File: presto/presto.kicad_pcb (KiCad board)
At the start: 2 copper layers, 110 x 110 mm, 61 parts, among them J101 12V IN, J301 ESTOP IN, J401 ESTOP SW, J701 LED Connector, K301 12V SRD Form C, K401 12V SRD Form C

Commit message: LED diode traces not connected properly, deleted, needs to be fixed
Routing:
- net /LED Interface/green: track 83.4 -> 162.4 mm
- net /LED Interface/yellow: track 83.7 -> 24.5 mm
- net /LED Interface/red: track 77.4 -> 32.7 mm
- net /LED Interface/blue: track 78.3 -> 117.2 mm
- net /EStop Reading/estop_signal: track 79.6 -> 78.7 mm
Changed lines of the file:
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@@
 	)
 	(gr_text "6 mm apart"
-		(at 61.595 139.7 0)
+		(at 55.245 141.605 0)
 		(layer "F.Cu")
 		(effects
@@
 	)
 	(segment
-		(start 123.825 120.65)
-		(end 130.175 120.65)
-		(width 0.2)
-		(layer "B.Cu")
-		(net 1)
-	)
-	(segment
-		(start 130.175 120.65)
-		(end 144.78 135.255)
-		(width 0.2)
-		(layer "B.Cu")
-		(net 1)
-	)
-	(segment
-		(start 108.75 114.3)
-		(end 117.475 114.3)
-		(width 0.2)
-		(layer "B.Cu")
-		(net 1)
-	)
-	(segment
-		(start 117.475 114.3)
-		(end 123.825 120.65)
-		(width 0.2)
-		(layer "B.Cu")
-		(net 1)
+		(start 102.921 153.721)
+		(end 101.6 152.4)
+		(width 0.2)
+		(layer "F.Cu")
+		(net 4)
 	)
 	(segment
@@
 	)
 	(segment
+		(start 152.42391 153.721)
+		(end 102.921 153.721)
+		(width 0.2)
+		(layer "F.Cu")
+		(net 4)
+	)
+	(segment
+		(start 104.14 124.46)
+		(end 107.95 124.46)
+		(width 0.2)
+		(layer "F.Cu")
+		(net 4)
+	)
+	(segment
+		(start 101.6 152.4)
+		(end 101.6 127)
+		(width 0.2)
+		(layer "F.Cu")
+		(net 4)
+	)
+	(segment
+		(start 165.655 140.48991)
+		(end 152.42391 153.721)
+		(width 0.2)
+		(layer "F.Cu")
+		(net 4)
+	)
+	(segment
+		(start 165.655 135.00625)
+		(end 165.655 140.48991)
+		(width 0.2)
+		(layer "F.Cu")
+		(net 4)
+	)
+	(segment
+		(start 101.6 127)
+		(end 104.14 124.46)
+		(width 0.2)
+		(layer "F.Cu")
+		(net 4)
+	)
+	(segment
 		(start 165.655 135.00625)
 		(end 169.85125 130.81)
@@
 	)
 	(segment
-		(start 118.11 128.905)
-		(end 113.665 124.46)
-		(width 0.2)
-		(layer "B.Cu")
-		(net 4)
-	)
-	(segment
-		(start 124.46 140.97)
-		(end 118.11 134.62)
-		(width 0.2)
-		(layer "B.Cu")
-		(net 4)
-	)
-	(segment
-		(start 113.665 124.46)
-		(end 108.75 124.46)
-		(width 0.2)
-		(layer "B.Cu")
-		(net 4)
-	)
-	(segment
-		(start 165.1 135.89)
-		(end 163.83 135.89)
-		(width 0.2)
-		(layer "B.Cu")
-		(net 4)
-	)
-	(segment
-		(start 163.83 135.89)
-		(end 158.75 140.97)
-		(width 0.2)
-		(layer "B.Cu")
-		(net 4)
-	)
-	(segment
-		(start 158.75 140.97)
-		(end 124.46 140.97)
-		(width 0.2)
-		(layer "B.Cu")
-		(net 4)
-	)
-	(segment
-		(start 118.11 134.62)
-		(end 118.11 128.905)
-		(width 0.2)
-		(layer "B.Cu")
-		(net 4)
-	)
-	(segment
-		(start 165.735 135.255)
-		(end 165.1 135.89)
-		(width 0.2)
-		(layer "B.Cu")
-		(net 4)
-	)
-	(segment
 		(start 120.65 48.895)
 		(end 128.27 56.515)
@@
 	)
 	(segment
-		(start 121.92 121.285)
-		(end 121.92 131.445)
-		(width 0.2)
-		(layer "B.Cu")
-		(net 8)
-	)
-	(segment
-		(start 121.92 133.985)
-		(end 123.825 135.89)
-		(width 0.2)
-		(layer "B.Cu")
-		(net 8)
-	)
-	(segment
-		(start 123.825 135.89)
-		(end 151.765 135.89)
-		(width 0.2)
-		(layer "B.Cu")
-		(net 8)
-	)
-	(segment
-		(start 121.92 131.445)
-		(end 121.92 133.985)
-		(width 0.2)
-		(layer "B.Cu")
-		(net 8)
-	)
-	(segment
-		(start 108.75 116.84)
-		(end 117.475 116.84)
-		(width 0.2)
-		(layer "B.Cu")
-		(net 8)
-	)
-	(segment
-		(start 151.765 135.89)
-		(end 152.4 135.255)
-		(width 0.2)
-		(layer "B.Cu")
-		(net 8)
-	)
-	(segment
-		(start 117.475 116.84)
-		(end 121.92 121.285)
-		(width 0.2)
-		(layer "B.Cu")
-		(net 8)
+		(start 164.23475 129.659)
+		(end 173.19676 129.659)
+		(width 0.2)
+		(layer "F.Cu")
+		(net 11)
+	)
+	(segment
+		(start 166.5435 142.280534)
+		(end 166.5435 143.48641)
+		(width 0.2)
+		(layer "F.Cu")
+		(net 11)
 	)
 	(segment
@@
 	)
 	(segment
+		(start 173.19676 129.659)
+		(end 173.871 130.33324)
+		(width 0.2)
+		(layer "F.Cu")
+		(net 11)
+	)
+	(segment
+		(start 155.90791 154.122)
+		(end 98.877 154.122)
+		(width 0.2)
+		(layer "F.Cu")
+		(net 11)
+	)
+	(segment
+		(start 173.871 130.33324)
+		(end 173.871 134.953034)
+		(width 0.2)
+		(layer "F.Cu")
+		(net 11)
+	)
+	(segment
 		(start 165.62375 128.27)
 		(end 172.72 128.27)
@@
 	)
 	(segment
-		(start 118.11 119.38)
-		(end 120.65 121.92)
-		(width 0.2)
-		(layer "B.Cu")
-		(net 11)
-	)
-	(segment
-		(start 155.406 138.599)
-		(end 158.75 135.255)
-		(width 0.2)
-		(layer "B.Cu")
-		(net 11)
-	)
-	(segment
-		(start 120.65 134.62)
-		(end 124.629 138.599)
-		(width 0.2)
-		(layer "B.Cu")
-		(net 11)
-	)
-	(segment
-		(start 108.75 119.38)
-		(end 118.11 119.38)
-		(width 0.2)
-		(layer "B.Cu")
-		(net 11)
-	)
-	(segment
-		(start 124.629 138.599)
-		(end 155.406 138.599)
-		(width 0.2)
-		(layer "B.Cu")
-		(net 11)
-	)
-	(segment
-		(start 120.65 121.92)
-		(end 120.65 134.62)
-		(width 0.2)
-		(layer "B.Cu")
+		(start 158.8875 135.00625)
+		(end 164.23475 129.659)
+		(width 0.2)
+		(layer "F.Cu")
+		(net 11)
+	)
+	(segment
+		(start 158.8875 135.00625)
+		(end 158.8875 135.1175)
+		(width 0.2)
+		(layer "F.Cu")
+		(net 11)
+	)
+	(segment
+		(start 98.877 154.122)
+		(end 97.155 152.4)
+		(width 0.2)
+		(layer "F.Cu")
+		(net 11)
+	)
+	(segment
+		(start 173.871 134.953034)
+		(end 166.5435 142.280534)
+		(width 0.2)
+		(layer "F.Cu")
+		(net 11)
+	)
+	(segment
+		(start 97.155 130.175)
+		(end 107.95 119.38)
+		(width 0.2)
+		(layer "F.Cu")
+		(net 11)
+	)
+	(segment
+		(start 97.155 152.4)
+		(end 97.155 130.175)
+		(width 0.2)
+		(layer "F.Cu")
+		(net 11)
+	)
+	(segment
+		(start 166.5435 143.48641)
+		(end 155.90791 154.122)
+		(width 0.2)
+		(layer "F.Cu")
 		(net 11)
 	)
@@
 	(segment
 		(start 92.075 86.36)
-		(end 92.71 85.725)
+		(end 93.993 84.442)
 		(width 0.2)
 		(layer "B.Cu")
@@
 	)
 	(segment
-		(start 93.993 84.442)
-		(end 92.075 86.36)
-		(width 0.254)
-		(layer "B.Cu")
-		(net 15)
-	)
-	(segment
 		(start 103.505 111.76)
 		(end 92.075 100.33)
@@
 	)
 	(segment
+		(start 138.43 62.865)
+		(end 148.62 52.675)
+		(width 0.254)
+		(layer "B.Cu")
+		(net 24)
+	)
+	(segment
 		(start 108.75 104.14)
 		(end 123.355 89.535)
@@
 	)
 	(segment
-		(start 148.59 52.705)
-		(end 148.59 52.07)
+		(start 138.43 89.535)
+		(end 138.43 62.865)
 		(width 0.254)
 		(layer "B.Cu")
@@
 	)
 	(segment
-		(start 138.43 62.865)
-		(end 148.59 52.705)
-		(width 0.254)
-		(layer "B.Cu")
-		(net 24)
-	)
-	(segment
-		(start 148.59 52.705)
-		(end 148.62 52.675)
-		(width 0.254)
-		(layer "B.Cu")
-		(net 24)
-	)
-	(segment
-		(start 138.43 89.535)
-		(end 138.43 62.865)
-		(width 0.254)
-		(layer "B.Cu")
-		(net 24)
-	)
-	(segment
-		(start 148.62 52.04)
-		(end 148.62 50.165)
-		(width 0.254)
-		(layer "B.Cu")
-		(net 24)
-	)
-	(segment
-		(start 148.59 52.07)
-		(end 148.62 52.04)
-		(width 0.254)
-		(layer "B.Cu")
-		(net 24)
-	)
-	(segment
 		(start 123.355 89.535)
 		(end 138.43 89.535)
 		(width 0.254)
 		(layer "B.Cu")
+		(net 24)
+	)
+	(segment
+		(start 148.62 52.675)
+		(end 148.62 50.165)
+		(width 0.254)
+		(layer "B.Cu")

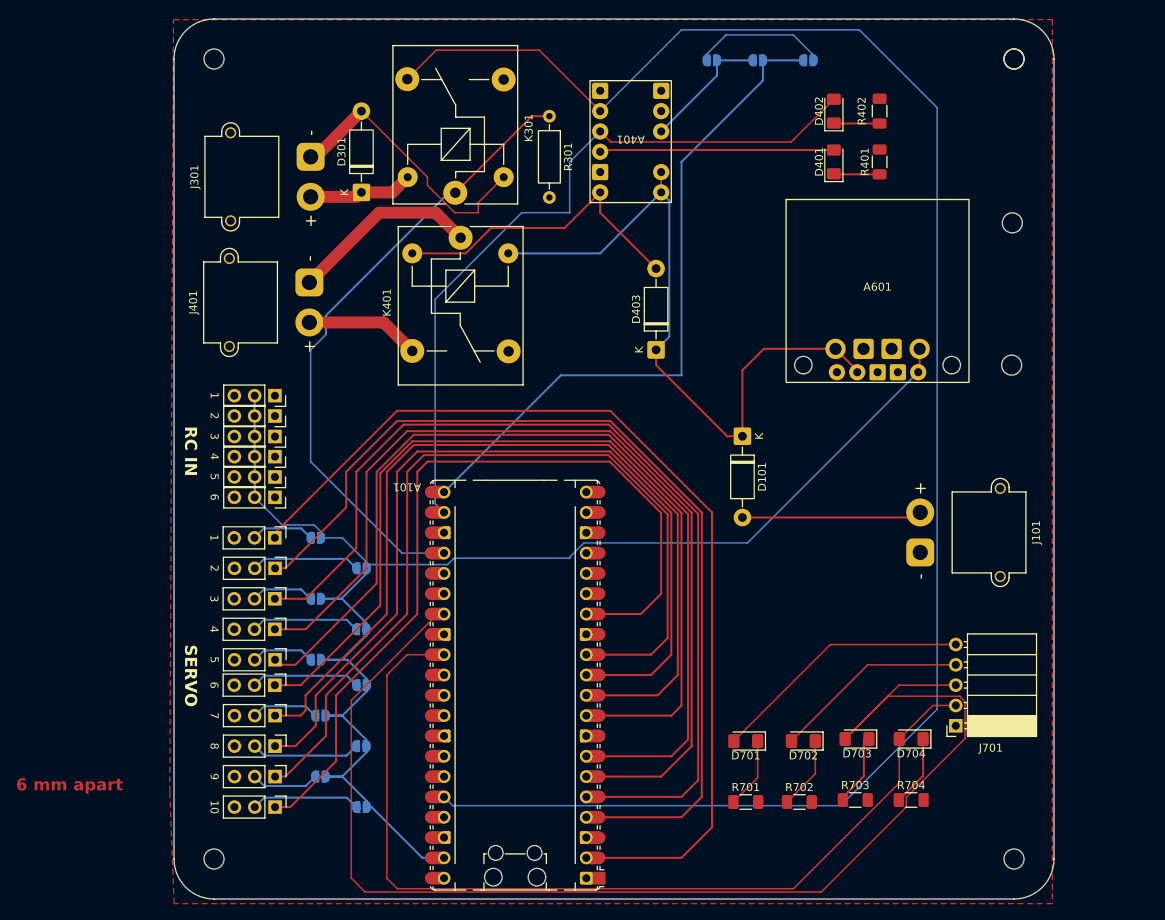
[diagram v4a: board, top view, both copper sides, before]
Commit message: Rearranged to accomodate JST
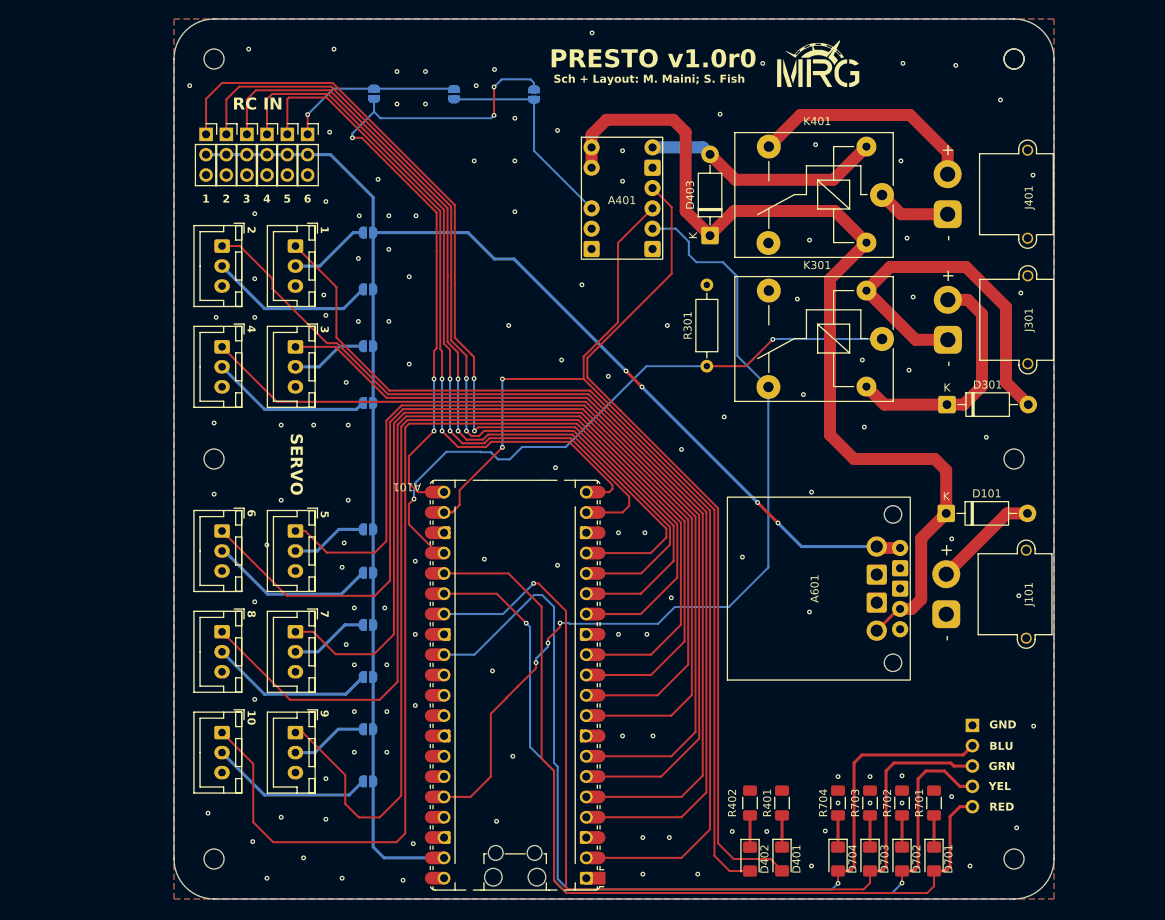
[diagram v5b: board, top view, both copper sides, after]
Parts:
- J201: renamed from 1; footprint Connector_PinHeader_2.54mm:PinHeader_1x03_P2.54mm_Vertical -> Connector_JST:JST_XH_B3B-XH-A_1x03_P2.50mm_Vertical
- J202: renamed from 2; footprint Connector_PinHeader_2.54mm:PinHeader_1x03_P2.54mm_Vertical -> Connector_JST:JST_XH_B3B-XH-A_1x03_P2.50mm_Vertical
- J203: renamed from 3; footprint Connector_PinHeader_2.54mm:PinHeader_1x03_P2.54mm_Vertical -> Connector_JST:JST_XH_B3B-XH-A_1x03_P2.50mm_Vertical
- J204: renamed from 4; footprint Connector_PinHeader_2.54mm:PinHeader_1x03_P2.54mm_Vertical -> Connector_JST:JST_XH_B3B-XH-A_1x03_P2.50mm_Vertical
- J205: renamed from 5; footprint Connector_PinHeader_2.54mm:PinHeader_1x03_P2.54mm_Vertical -> Connector_JST:JST_XH_B3B-XH-A_1x03_P2.50mm_Vertical
- J206: renamed from 6; footprint Connector_PinHeader_2.54mm:PinHeader_1x03_P2.54mm_Vertical -> Connector_JST:JST_XH_B3B-XH-A_1x03_P2.50mm_Vertical
- J207: renamed from 7; footprint Connector_PinHeader_2.54mm:PinHeader_1x03_P2.54mm_Vertical -> Connector_JST:JST_XH_B3B-XH-A_1x03_P2.50mm_Vertical
- J208: renamed from 8; footprint Connector_PinHeader_2.54mm:PinHeader_1x03_P2.54mm_Vertical -> Connector_JST:JST_XH_B3B-XH-A_1x03_P2.50mm_Vertical
- J209: renamed from 9; footprint Connector_PinHeader_2.54mm:PinHeader_1x03_P2.54mm_Vertical -> Connector_JST:JST_XH_B3B-XH-A_1x03_P2.50mm_Vertical
- J210: renamed from 10; footprint Connector_PinHeader_2.54mm:PinHeader_1x03_P2.54mm_Vertical -> Connector_JST:JST_XH_B3B-XH-A_1x03_P2.50mm_Vertical
- J701: moved to B.Cu
- moved REF** 104.1 mm to (80.0, 100.0)
- moved D402 94.1 mm to (147.0, 150.0), turned to -90 degrees
- moved R402 88.0 mm to (147.0, 143.0)
- moved D401 87.4 mm to (151.0, 150.0), turned to -90 degrees
- moved J301 82.9 mm to (171.7, 85.1), turned to -90 degrees
- moved R401 81.1 mm to (151.0, 143.0)
- moved J401 80.2 mm to (171.7, 69.4), turned to -90 degrees
- moved D301 77.9 mm to (171.6, 93.2), turned to 0 degrees
- moved K301 56.4 mm to (163.5, 85.0), turned to 180 degrees
- moved JP101 54.5 mm to (100.0, 54.4), turned to -90 degrees
- moved K401 52.9 mm to (163.5, 67.0), turned to 180 degrees
- moved J506 45.6 mm to (91.7, 59.4), turned to 0 degrees
- moved J505 42.9 mm to (89.2, 59.4), turned to 0 degrees
- moved J202 40.8 mm to (81.0, 73.4)
- moved J504 40.3 mm to (86.6, 59.4), turned to 0 degrees
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- renumbered 1 to J501, 2 to J502, 3 to J503, 4 to J504, 5 to J505, 6 to J506
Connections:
- A101 pad 15: unconnected-(A101-GPIO11-Pad15) -> /RC Interface/ch1
- A101 pad 16: unconnected-(A101-GPIO12-Pad16) -> /RC Interface/ch2
- A101 pad 17: unconnected-(A101-GPIO13-Pad17) -> /RC Interface/ch3
- A101 pad 19: unconnected-(A101-GPIO14-Pad19) -> /RC Interface/ch4
- A101 pad 20: unconnected-(A101-GPIO15-Pad20) -> /RC Interface/ch5
- JP101 pad 1: Net-(JP101-A) -> /RC Interface/ch6
- JP103 pad 1: Net-(JP101-A) -> /RC Interface/ch6
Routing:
- net /RC Interface/ch1: track 0.00 -> 118.4 mm, vias 0 -> 2
- net /RC Interface/ch2: track 0.00 -> 113.3 mm, vias 0 -> 2
- net +3V3: track 221.4 -> 110.7 mm, vias 0 -> 3
- net /RC Interface/ch3: track 0.00 -> 107.2 mm, vias 0 -> 2
- net /RC Interface/ch4: track 0.00 -> 93.2 mm, vias 0 -> 2
- net /LED Interface/yellow: track 24.5 -> 112.8 mm, vias 0 -> 2
- net /RC Interface/ch5: track 0.00 -> 84.8 mm, vias 0 -> 2
- net /LED Interface/red: track 32.7 -> 111.0 mm
- net Net-(A401-GOOD): track 29.3 -> 103.5 mm
- net /LED Interface/green: track 162.4 -> 118.3 mm, vias 0 -> 1
- net /Servo Interface/servo10: track 103.8 -> 142.6 mm
- net /gpio17: track 92.1 -> 127.0 mm, vias 0 -> 2
- net +12V: track 87.0 -> 120.9 mm
- net /Servo Interface/servo9: track 107.9 -> 133.0 mm
- net /RC Interface/ch6: track 0.00 -> 22.1 mm, vias 0 -> 1
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- added copper zone on B.Cu, net GND
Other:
- board text added: "1"
- board text added: "10"
- board text added: "12V IN"
- board text added: "2"
- board text added: "3"
- board text added: "4"
- board text added: "5"
- board text added: "6"
- board text added: "7"
- board text added: "8"
- board text added: "9"
- board text added: "BLU"
- board text added: "CH6-ES"
- board text added: "CH6-GP"
- board text added: "ESTOP SIGNAL"
- board text added: "ESTOP TRIGGER"
- board text added: "GND"
- board text added: "GP-ES"
- board text added: "GRN"
- board text added: "PRESTO v1.0r0"
- board text added: "RED"
- board text added: "Sch + Layout: M. Maini; S. Fish"
- board text added: "YEL"
- board text removed: "6 mm apart"

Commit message: Fixed double hole
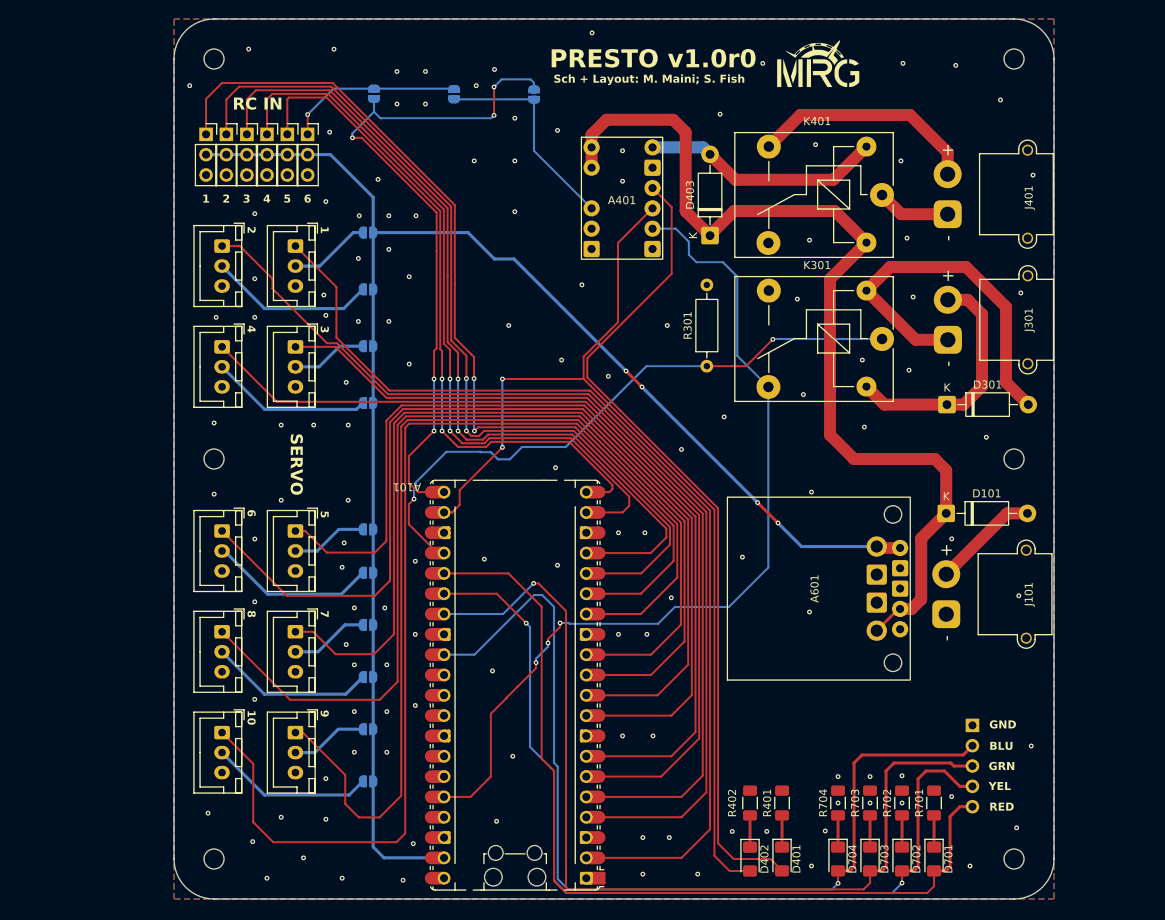
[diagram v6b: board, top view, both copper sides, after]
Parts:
- removed ?: , 
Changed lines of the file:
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@@
 		)
 	)
-	(footprint ""
-		(layer "F.Cu")
-		(at 180 50)
-		(property "Reference" ""
-			(at 0 0 0)
-			(layer "F.SilkS")
-			(effects
-				(font
-					(size 1.27 1.27)
-					(thickness 0.15)
-				)
-			)
-		)
-		(property "Value" ""
-			(at 0 0 0)
-			(layer "F.Fab")
-			(effects
-				(font
-					(size 1.27 1.27)
-					(thickness 0.15)
-				)
-			)
-		)
-		(property "Datasheet" ""
-			(at 0 0 0)
-			(layer "F.Fab")
-			(hide yes)
-			(effects
-				(font
-					(size 1.27 1.27)
-					(thickness 0.15)
-				)
-			)
-		)
-		(property "Description" ""
-			(at 0 0 0)
-			(layer "F.Fab")
-			(hide yes)
-			(effects
-				(font
-					(size 1.27 1.27)
-					(thickness 0.15)
-				)
-			)
-		)
-		(pad "" np_thru_hole circle
-			(at 0 0)
-			(size 2.5 2.5)
-			(drill 2.5)
-			(layers "*.Cu" "*.Mask")
-		)
-		(embedded_fonts no)
-	)
 	(footprint "Connector_PinSocket_2.54mm:PinSocket_1x03_P2.54mm_Vertical"
 		(layer "F.Cu")
@@
 	)
 	(via
-		(at 182.45 133.389045)
+		(at 182.15 135.875)
 		(size 0.6)
 		(drill 0.3)
@@
 	)
 	(via
-		(at 86.614 110.744)
+		(at 85.1 110)
 		(size 0.6)
 		(drill 0.3)
